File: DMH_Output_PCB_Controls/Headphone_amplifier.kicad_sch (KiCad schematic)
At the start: 26 parts, among them J12 Conn_01x06_PinHeader, J27 Conn_01x06_PinHeader, U11 TL074, U12 NE5532, U13 NE5532, U14 NE5532, U15 NE5532

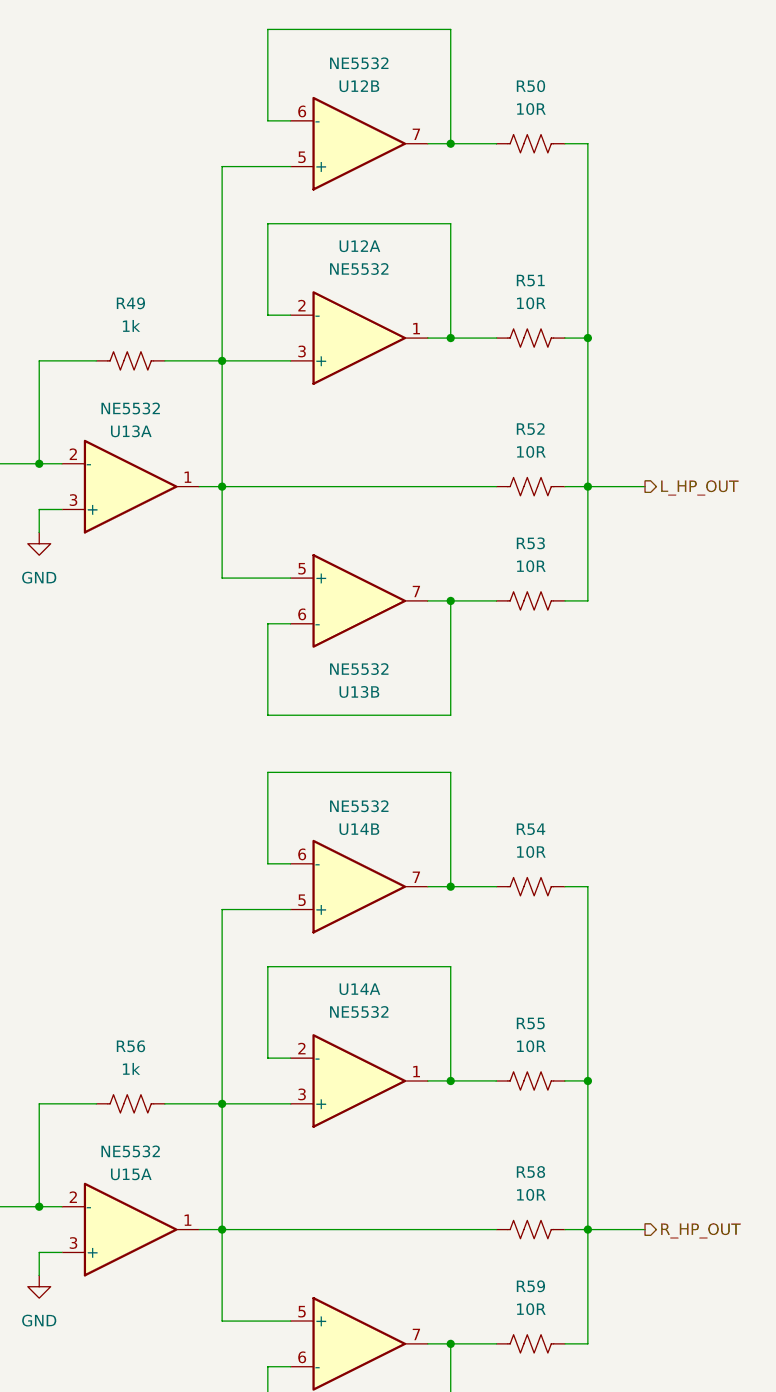
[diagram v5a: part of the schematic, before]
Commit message: Removed 2 extra OpAmps from the headphone amp
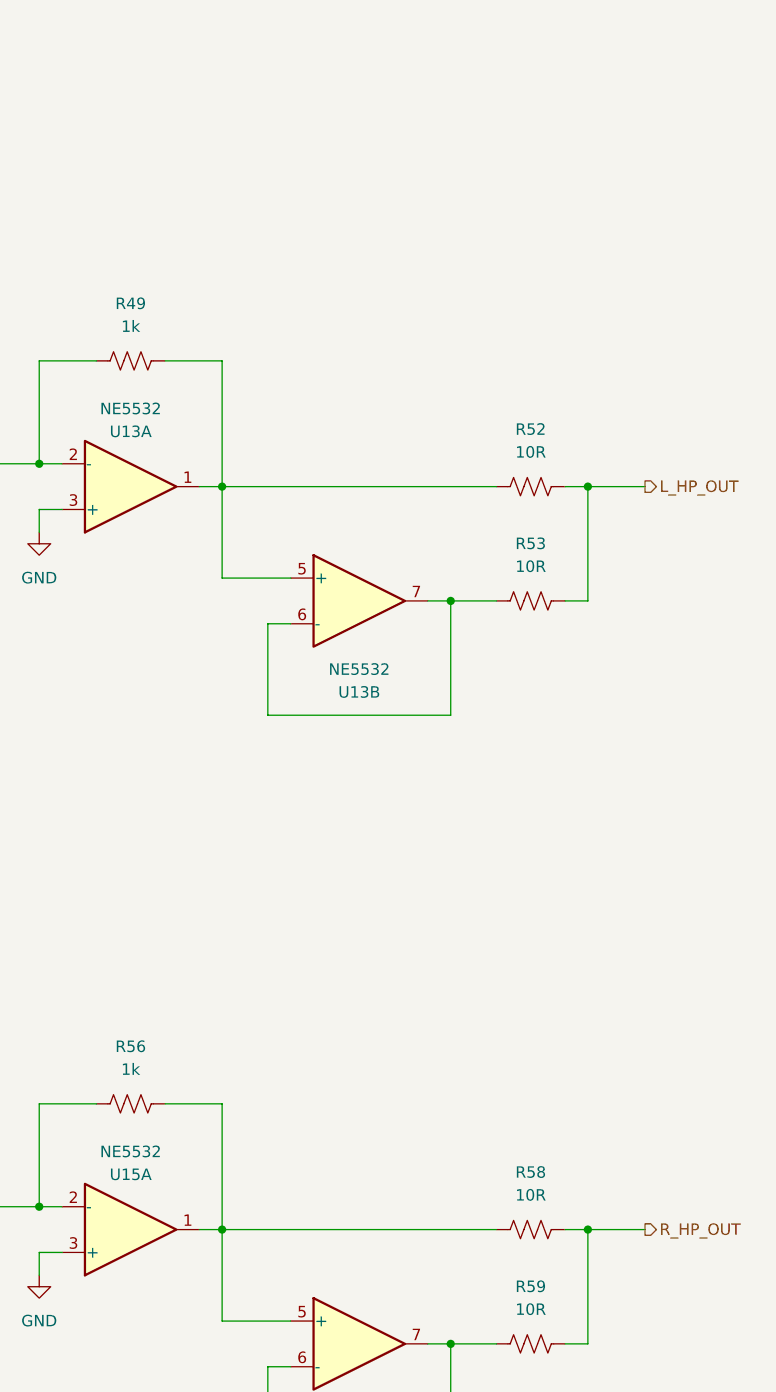
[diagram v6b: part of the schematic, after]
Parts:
- removed R50, R51, R54, R55: 10R, Resistor_THT:R_Axial_DIN0207_L6.3mm_D2.5mm_P7.62mm_Horizontal, symbol Device:R_US
- removed U12, U14: NE5532, Package_DIP:DIP-8_W7.62mm_Socket, symbol Amplifier_Operational:NE5532

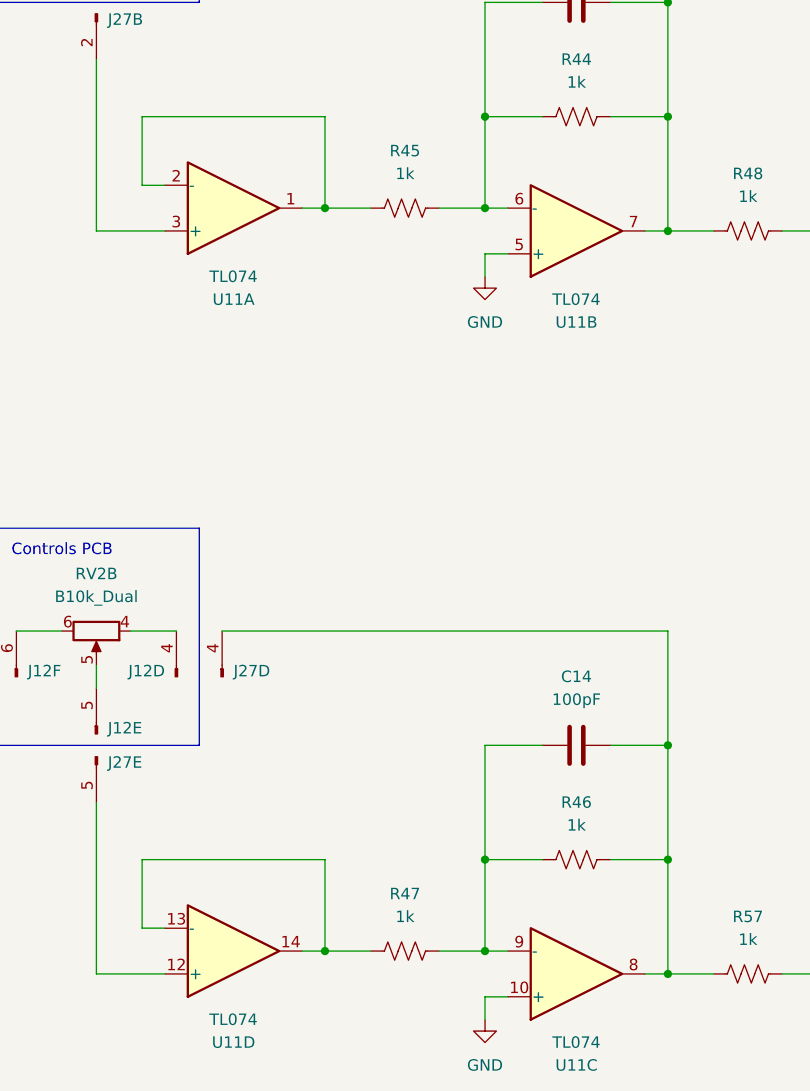
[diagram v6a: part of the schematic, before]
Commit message: Changed headphone amp max gain
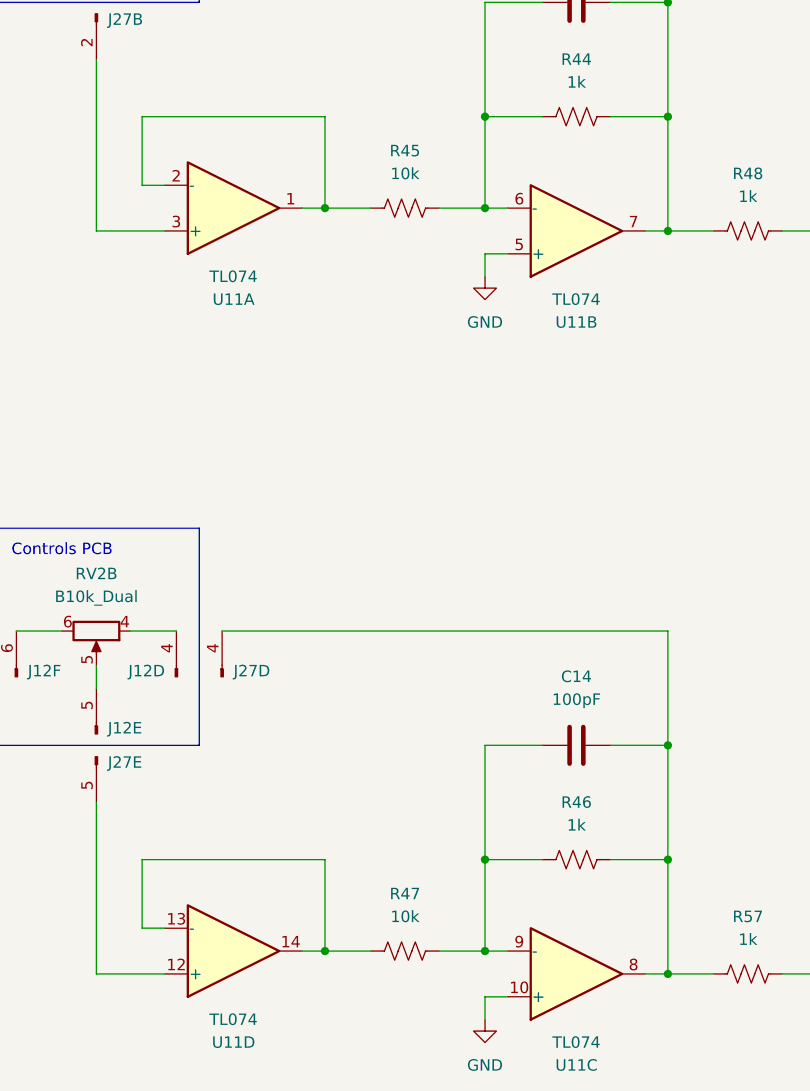
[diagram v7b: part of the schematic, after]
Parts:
- R45, R47: value 1k -> 10k
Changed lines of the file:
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@@
 			)
 		)
-		(property "Value" "1k"
+		(property "Value" "10k"
 			(at 76.2 57.15 90)
 			(show_name no)
@@
 			)
 		)
-		(property "Value" "1k"
+		(property "Value" "10k"
 			(at 76.2 139.7 90)
 			(show_name no)

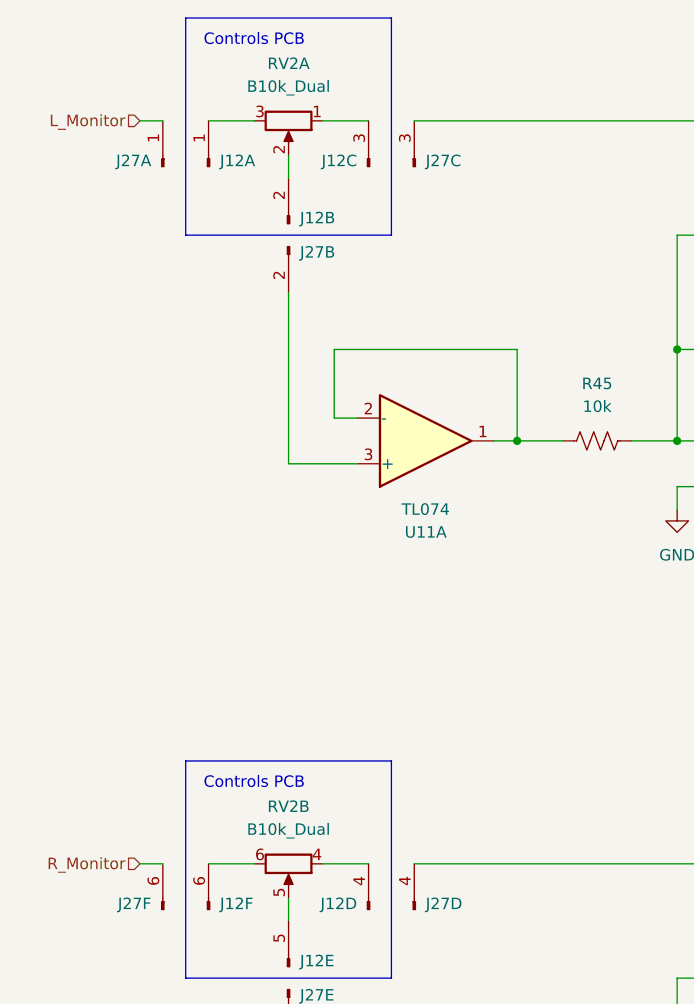
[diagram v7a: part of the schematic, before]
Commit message: Replaced jack symbols with 5pin ones
Also updated Meter LED current source resistor to 75R
Also increased LED guiding PCB mounting holes to M2.5
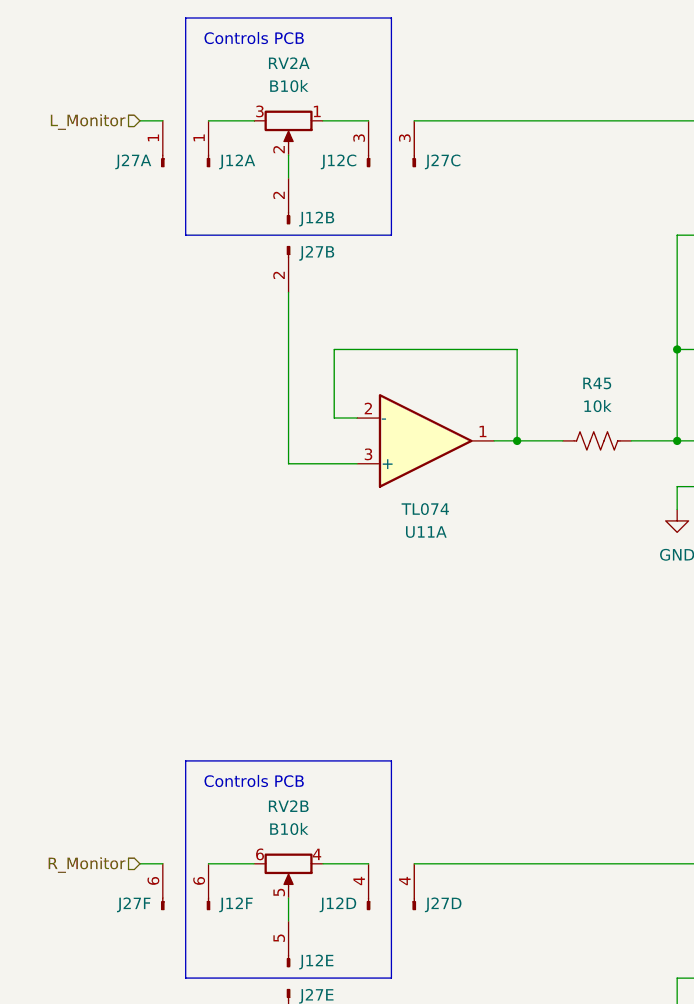
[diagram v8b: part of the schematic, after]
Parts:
- RV2: value B10k_Dual -> B10k; footprint Potentiometer_THT:Potentiometer_Alpha_RD902F-40-00D_Dual_Vertical -> SynthStuff:Potentiometer_Alpha_RD902F-40-00D_Dual_Vertical
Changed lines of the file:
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@@
 			)
 		)
-		(property "Value" "B10k_Dual"
+		(property "Value" "B10k"
 			(at 41.91 104.14 90)
 			(show_name no)
@@
 			)
 		)
-		(property "Footprint" "Potentiometer_THT:Potentiometer_Alpha_RD902F-40-00D_Dual_Vertical"
+		(property "Footprint" "SynthStuff:Potentiometer_Alpha_RD902F-40-00D_Dual_Vertical"
 			(at 41.91 107.95 0)
 			(hide yes)
@@
 					(bold yes)
 					(italic yes)
+				)
+			)
+		)
+		(property "Sim.Library" "${KICAD9_SYMBOL_DIR}/Simulation_SPICE.sp"
+			(at 41.91 107.95 0)
+			(hide yes)
+			(show_name no)
+			(do_not_autoplace no)
+			(effects
+				(font
+					(size 1.27 1.27)
+				)
+			)
+		)
+		(property "Sim.Name" "pot_dual"
+			(at 41.91 107.95 0)
+			(hide yes)
+			(show_name no)
+			(do_not_autoplace no)
+			(effects
+				(font
+					(size 1.27 1.27)
+				)
+			)
+		)
+		(property "Sim.Device" "SUBCKT"
+			(at 41.91 107.95 0)
+			(hide yes)
+			(show_name no)
+			(do_not_autoplace no)
+			(effects
+				(font
+					(size 1.27 1.27)
+				)
+			)
+		)
+		(property "Sim.Pins" "1=r1A 2=wA 3=r0A 4=r1B 5=wB 6=r0B"
+			(at 41.91 107.95 0)
+			(hide yes)
+			(show_name no)
+			(do_not_autoplace no)
+			(effects
+				(font
+					(size 1.27 1.27)
+				)
+			)
+		)
+		(property "Sim.Params" "Rtot=1 wpos=0.4"
+			(at 41.91 107.95 0)
+			(hide yes)
+			(show_name no)
+			(do_not_autoplace no)
+			(effects
+				(font
+					(size 1.27 1.27)
 				)
 			)
@@
 			)
 		)
-		(property "Value" "B10k_Dual"
+		(property "Value" "B10k"
 			(at 41.91 21.59 90)
 			(show_name no)
@@
 			)
 		)
-		(property "Footprint" "Potentiometer_THT:Potentiometer_Alpha_RD902F-40-00D_Dual_Vertical"
+		(property "Footprint" "SynthStuff:Potentiometer_Alpha_RD902F-40-00D_Dual_Vertical"
 			(at 41.91 25.4 0)
 			(hide yes)
@@
 				)
 			)
+		)
+		(property "Sim.Library" "${KICAD9_SYMBOL_DIR}/Simulation_SPICE.sp"
+			(at 41.91 25.4 0)
+			(hide yes)
+			(show_name no)
+			(do_not_autoplace no)
+			(effects
+				(font
+					(size 1.27 1.27)
+				)
+			)
+		)
+		(property "Sim.Name" "pot_dual"
+			(at 41.91 25.4 0)
+			(hide yes)
+			(show_name no)
+			(do_not_autoplace no)
+			(effects
+				(font
+					(size 1.27 1.27)
+				)
+			)
+		)
+		(property "Sim.Device" "SUBCKT"
+			(at 41.91 25.4 0)
+			(hide yes)
+			(show_name no)
+			(do_not_autoplace no)
+			(effects
+				(font
+					(size 1.27 1.27)
+				)
+			)
+		)
+		(property "Sim.Pins" "1=r1A 2=wA 3=r0A 4=r1B 5=wB 6=r0B"
+			(at 41.91 25.4 0)
+			(hide yes)
+			(show_name no)
+			(do_not_autoplace no)
+			(effects
+				(font
+					(size 1.27 1.27)
+				)
+			)
+		)
+		(property "Sim.Params" "Rtot=1 wpos=0.4"
+			(at 41.91 25.4 0)
+			(hide yes)
+			(show_name no)
+			(do_not_autoplace no)
+			(effects
+				(font
+					(size 1.27 1.27)
+				)
+			)
